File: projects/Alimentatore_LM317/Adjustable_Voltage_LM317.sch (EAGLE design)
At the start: 17 parts, among them X1 SMKDSP_1,5/3, X2 SMKDSP_1,5/3, X3 SMKDSP_1,5/3

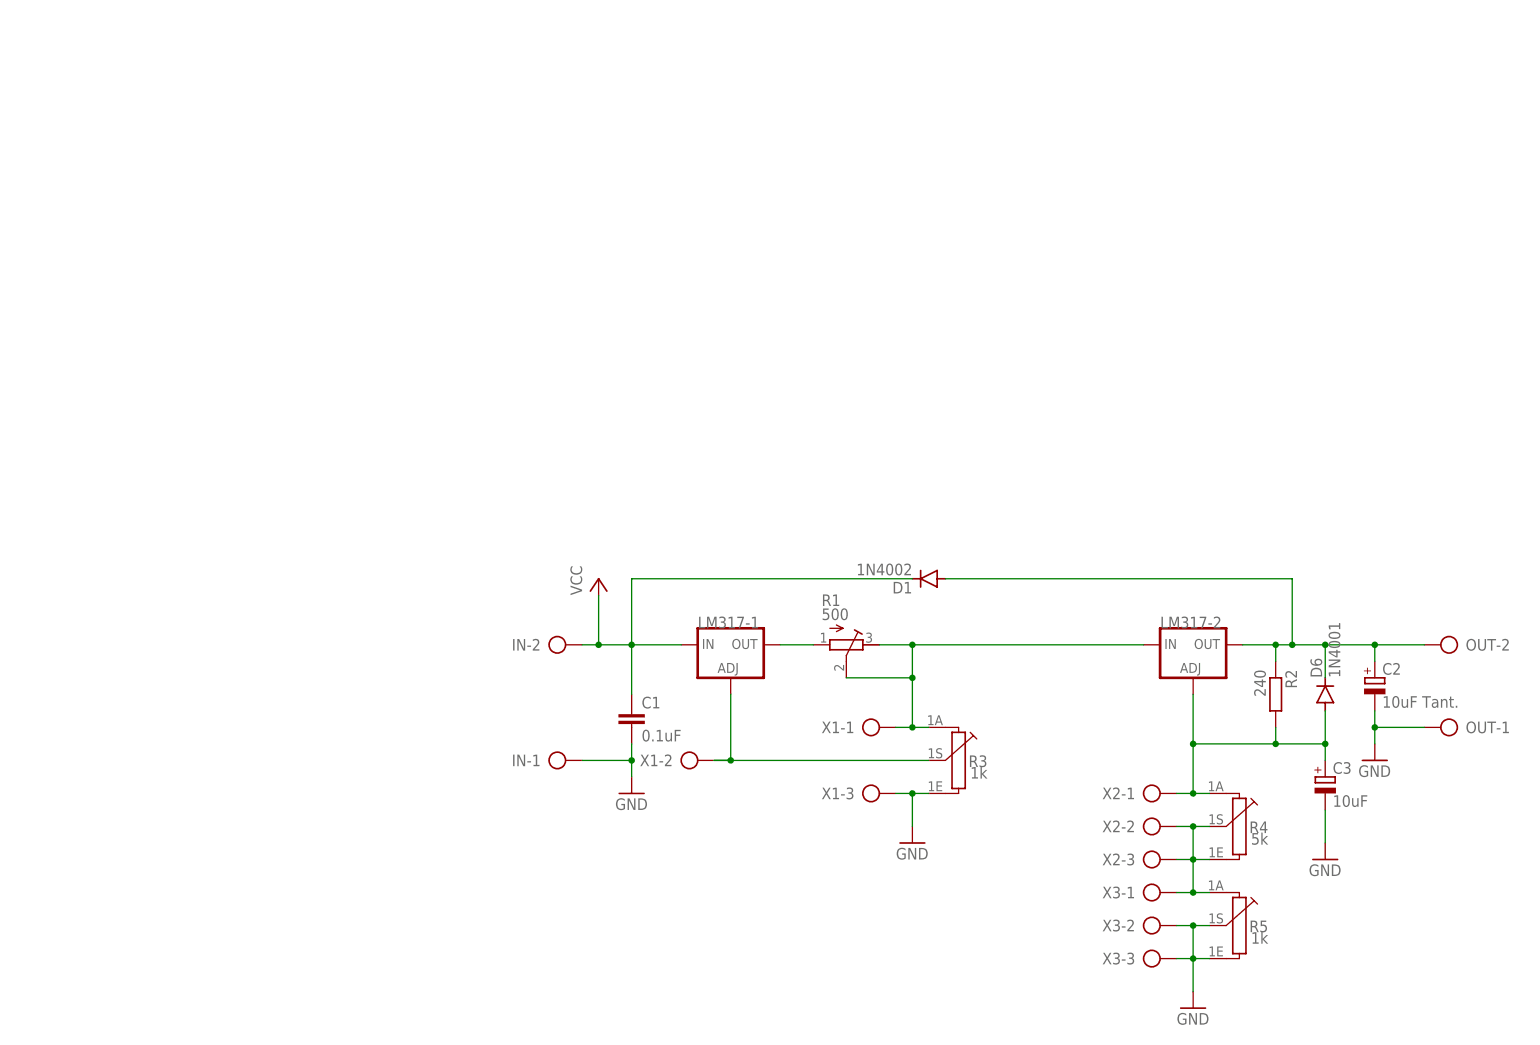
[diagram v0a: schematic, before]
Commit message: aggiunti circuiti alternativi LM317.
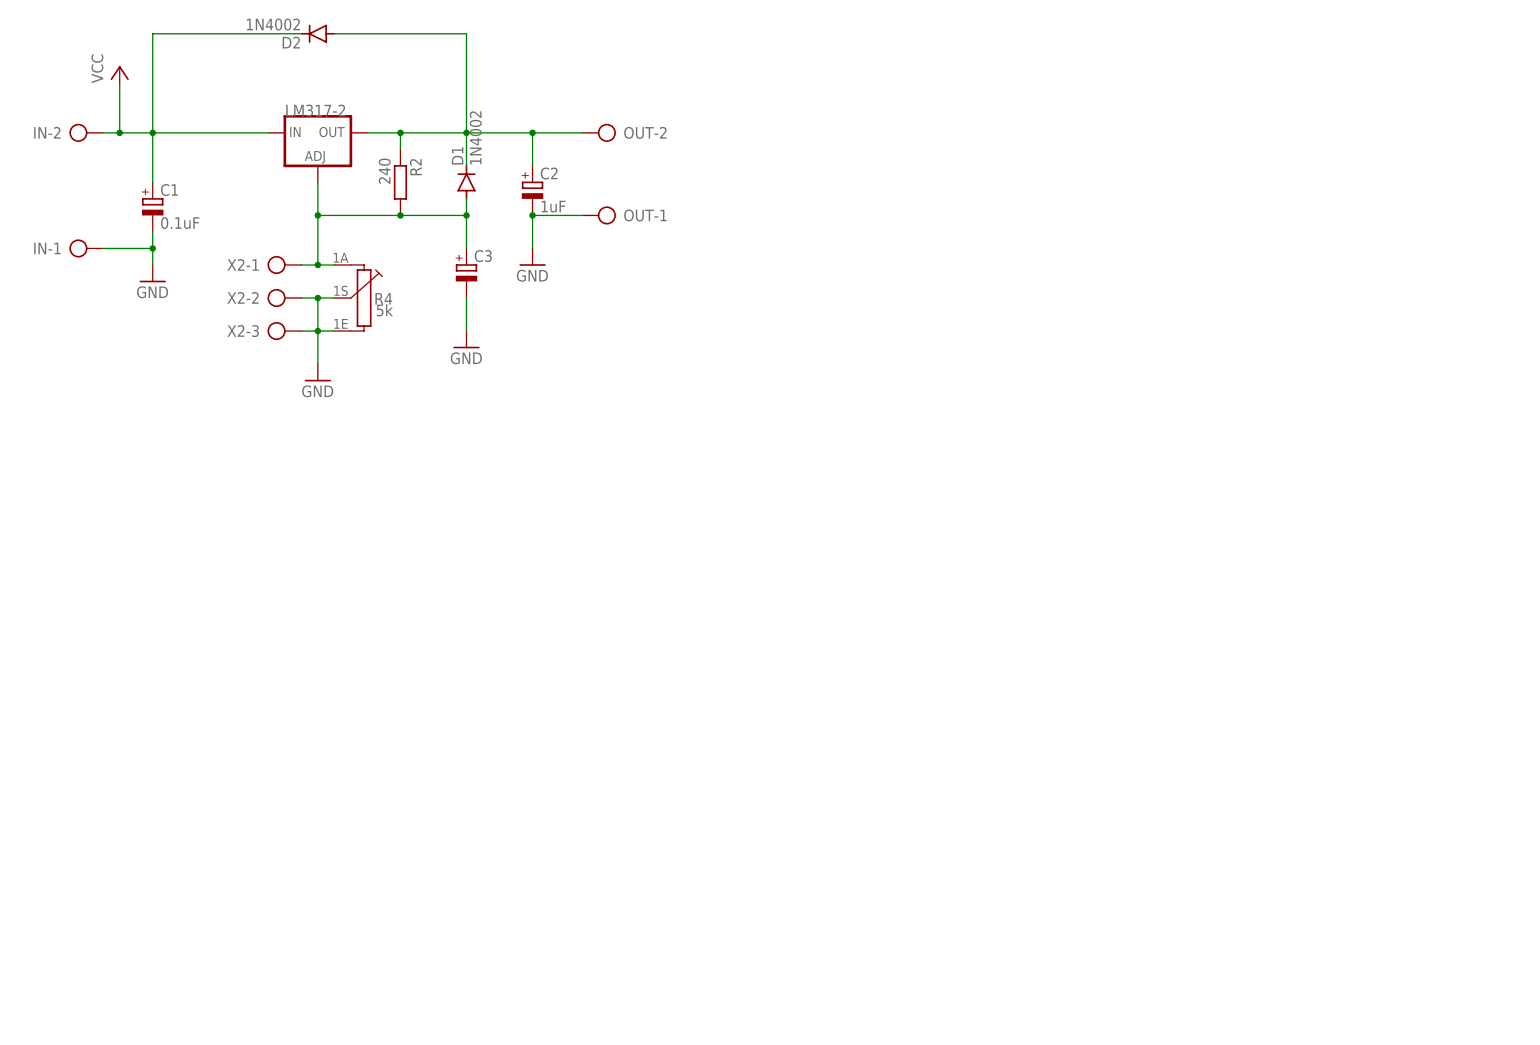
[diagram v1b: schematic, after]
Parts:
- removed D6: 1N4001, diode_MOD:1N4004DO-41
- removed LM317-1: (no value), v-reg:LM317TS317TS_TO220
- removed R1: 500, rcl:R-TRIMM4G/J
- removed R3, R5: 1k, piher:PC16S
- removed X1, X3: SMKDSP_1,5/3, con-phoenix-smkdsp:SMKDSP_1,5/3
- added D2: 1N4002, diode_MOD:1N4004DO-41
- C1: device rcl:C-EU025-024X044 -> rcl:CPOL-EUE2-5
- C2: value 10uF Tant. -> 1uF
- C3: value 10uF -> (none)
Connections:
- removed net N$3: LM317-2.IN, R1.E, R1.S, R3.1A, X1-1.KL
- removed net N$4: R4.1E, R4.1S, R5.1A, X2-2.KL, X2-3.KL, X3-1.KL
- removed net N$5: LM317-1.ADJ, R3.1S, X1-2.KL
- removed net VCC: C1.1, D1.C, IN-2.KL, LM317-1.IN
- net GND: now also C1.-, R4.1E, R4.1S, X2-2.KL, X2-3.KL; no longer C1.2, R3.1E, R5.1E, R5.1S, X1-3.KL, X3-2.KL, X3-3.KL
- net N$1: now also D1.C, D2.A; no longer D1.A, D6.C
- net N$2: now also C1.+, D2.C, IN-2.KL, LM317-2.IN; no longer LM317-1.OUT, R1.A
- net N$9: now also D1.A; no longer D6.A
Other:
- moved on the sheet: C2, C3, D1, IN-1, IN-2, LM317-2, OUT-1, OUT-2, R2, R4, X2-1, X2-2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
